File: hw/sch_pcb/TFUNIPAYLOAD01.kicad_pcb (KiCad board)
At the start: 4 copper layers, 90.9 x 50.3 mm, 71 parts, among them J1 SM08B-GHS-TB, J2 HEADER_2x15, J22 HEADER_2x03, J3 SM06B-GHS-TB, J7 SM03B-GHS-TB, M1 HOLE, M2 HOLE, M3 HOLE, M4 HOLE, Q2 BC817-25, Q3 BC817-25, Q4 BC817-25, U10 ATMEGA1284P-AU, U12 MIC5504-3.3YM5-TR, Y1 8 MHz

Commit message: Update schematics. Resolve #2
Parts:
- removed C26, C27, C28, C31, C36, C46, C51: 100nF, Capacitor_SMD:C_0805_2012Metric
- removed C41, C49: 10uF, Capacitor_SMD:C_0805_2012Metric
- removed D11: BZX585-B5V6.115, Diode_SMD:D_SOD-523
- removed F2: SR010-15 100mA, Fuse:Fuse_0805_2012Metric
- removed J22: HEADER_2x03, Mlab_Pin_Headers:SMD_2x03
- removed JP4: Jumper_2_Bridged, NetTie:NetTie-2_SMD_Pad0.5mm
- removed the L1 at (158.5, 101.8)
- removed TP5: Analog GND, TestPoint:TestPoint_Pad_D1.0mm
- removed U12: MIC5504-3.3YM5-TR, Package_TO_SOT_SMD:SOT-23-5
- added C13: 22u, Capacitor_SMD:C_0805_2012Metric, F.Cu at (125.5, 147.2)
- added C14: 47u, Capacitor_SMD:C_0805_2012Metric, F.Cu at (125.5, 150.2)
- added C15: 10u, Capacitor_SMD:C_0805_2012Metric, F.Cu at (125.5, 153.2)
- added C5: 22u, Capacitor_SMD:C_0805_2012Metric, F.Cu at (125.5, 138.1)
- added C6: 47u, Capacitor_SMD:C_0805_2012Metric, F.Cu at (125.5, 141.2)
- added C7: 10u, Capacitor_SMD:C_0805_2012Metric, F.Cu at (125.5, 144.2)
- added D7: RED, LED_SMD:LED_1206_3216Metric, F.Cu at (134.6, 162.0)
- added J3: HEADER_2x03, Mlab_Pin_Headers:SMD_2x03, F.Cu at (134.9, 155.9)
- added J4: SM04B-GHS-TB, Connector_JST:JST_GH_SM04B-GHS-TB_1x04-1MP_P1.25mm_Horizontal, F.Cu at (133.0, 147.8)
- added J6: SM07B-GHS-TB, Connector_JST:JST_GH_SM07B-GHS-TB_1x07-1MP_P1.25mm_Horizontal, F.Cu at (134.9, 140.4)
- added L2: 1uH - DFE252012P-1R0M=P2, Inductor_SMD:L_1008_2520Metric, F.Cu at (145.4, 153.4)
- added L3: 1uH - DFE252012P-1R0M=P2, Inductor_SMD:L_1008_2520Metric, F.Cu at (145.4, 157.2)
- added R10: 511k, Resistor_SMD:R_0805_2012Metric, F.Cu at (121.1, 144.0)
- added R11: 91k, Resistor_SMD:R_0805_2012Metric, F.Cu at (121.1, 147.0)
- added R2: 10k, Resistor_SMD:R_0805_2012Metric, F.Cu at (121.1, 138.1)
- added R22: 806k, Resistor_SMD:R_0805_2012Metric, F.Cu at (121.1, 149.9)
- added R23: 91k, Resistor_SMD:R_0805_2012Metric, F.Cu at (121.1, 152.9)
- added R24: 180R, Resistor_SMD:R_0805_2012Metric, F.Cu at (121.1, 155.8)
- added R25: 100R, Resistor_SMD:R_0603_1608Metric, F.Cu at (129.8, 152.8)
- added R26: 10k, Resistor_SMD:R_0805_2012Metric, F.Cu at (121.1, 158.8)
- added R27: 100R, Resistor_SMD:R_0603_1608Metric, F.Cu at (129.8, 155.3)
- added R28: 100R, Resistor_SMD:R_0603_1608Metric, F.Cu at (129.8, 157.8)
- added R29: 100R, Resistor_SMD:R_0603_1608Metric, F.Cu at (129.8, 160.3)
- added R3: 10k, Resistor_SMD:R_0805_2012Metric, F.Cu at (121.1, 141.1)
- added R30: 100R, Resistor_SMD:R_0603_1608Metric, F.Cu at (129.8, 162.8)
- added SW1: SKRTLAE010, Mlab_SW:SKRT, F.Cu at (141.3, 145.9)
- added SW2: KMT031, Mlab_SW:KMT031 NGJ LHS C&K, F.Cu at (140.4, 153.5)
- added SW3: KMT031, Mlab_SW:KMT031 NGJ LHS C&K, F.Cu at (140.4, 157.5)
- added U1: TPS631000DRLR, Package_TO_SOT_SMD:SOT-583-8, F.Cu at (139.8, 161.5)
- added U3: TPS631000DRLR, Package_TO_SOT_SMD:SOT-583-8, F.Cu at (143.5, 161.5)
- renumbered C38 to C1, C34 to C10, C35 to C11, C39 to C12, C43 to C2, C30 to C3, C33 to C4, C40 to C8, C44 to C9, D6 to D1, D1 to D2, D9 to D3, D7 to D4, D10 to D5, D8 to D6, J3 to J1, J1 to J2, J2 to J5, L2 to L1, Q4 to Q1, R33 to R1, R20 to R12, R21 to R13, R38 to R14, R43 to R15, R37 to R16, R32 to R17, R41 to R18, R45 to R19, R46 to R20, R47 to R21, R34 to R4, R23 to R5, R44 to R6, R42 to R7, R36 to R8, R35 to R9, TP6 to TP1, TP7 to TP2, U10 to U2
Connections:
- net /5v renamed +5V
- net /External_5V renamed Net-(D1-A)
- net /Signal_S&H renamed /EXT_A0
- net /Trace renamed /EXT_B0
- net /Virtual_ground renamed /EXT_A1
- C8 pad 2: GNDA -> GND
- C9 pad 2: GNDA -> GND
- D1 pad 1: Net-(D6-K) (its old number) -> Net-(D1-K)
- J5 pad 10: /RST -> /~{RST}_EXT
- J5 pad 5: /3v3 -> +3.3V
- J5 pad 6: /3v3 -> +3.3V
- J5 pad 8: /connection_detector -> /EXT_DETECTION
- L1 pad 2: Net-(U12-EN) -> +VSW
- U2 pad 1: /PB5 -> /MOSI
- U2 pad 16: POWER_ANALOG_3V3 -> unconnected-(U2-(PCINT31/OC2A)PD7-Pad16)
- U2 pad 2: /PB6 -> /MISO
- U2 pad 3: /PB7 -> /SCLK
- U2 pad 30: unconnected-(U10-(PCINT7/ADC7)PA7-Pad30) -> /BTN_USER_B
- U2 pad 31: unconnected-(U10-(PCINT6/ADC6)PA6-Pad31) -> /BTN_USER_A
- U2 pad 32: unconnected-(U10-(PCINT5/ADC5)PA5-Pad32) -> /#RTS
- U2 pad 33: unconnected-(U10-(PCINT4/ADC4)PA4-Pad33) -> /#CTS
- U2 pad 34: unconnected-(U10-(PCINT3/ADC3)PA3-Pad34) -> /EXT_DETECTION
- U2 pad 35: /Signal -> unconnected-(U2-(PCINT2/ADC2)PA2-Pad35)
- U2 pad 41: unconnected-(U10-(PCINT9/CLKO/T1)PB1-Pad41) -> /EXT_B1
- U2 pad 43: unconnected-(U10-(PCINT11/AIN1/OC0)PB3-Pad43) -> /CS2
- U2 pad 44: /PB4 -> /CS1
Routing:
- net /PB6: track 45.2 -> 0.00 mm, vias 1 -> 0
- net /MISO: track 0.00 -> 45.2 mm, vias 0 -> 1
- net /SCLK: track 0.00 -> 38.0 mm, vias 0 -> 1
- net /PB7: track 38.0 -> 0.00 mm, vias 1 -> 0
- net unconnected-(U10-(PCINT9/CLKO/T1)PB1-Pad41): track 34.5 -> 0.00 mm, vias 2 -> 0
- net /EXT_B1: track 0.00 -> 34.5 mm, vias 0 -> 2
- net (no net): track 147.8 -> 167.7 mm, vias 16 -> 18
- net unconnected-(U2-(PCINT31/OC2A)PD7-Pad16): track 0.00 -> 17.0 mm, vias 0 -> 2
- net POWER_ANALOG_3V3: track 17.0 -> 0.00 mm, vias 2 -> 0
- net +5V: track 16.2 -> 0.00 mm, vias 1 -> 0
- net /PB4: track 8.02 -> 0.00 mm, vias 1 -> 0
- net /CS1: track 0.00 -> 8.02 mm, vias 0 -> 1
- net unconnected-(U2-(PCINT2/ADC2)PA2-Pad35): track 0.00 -> 7.30 mm, vias 0 -> 2
- net /Signal: track 7.30 -> 0.00 mm, vias 2 -> 0
- net /3v3: track 3.79 -> 0.00 mm, vias 1 -> 0
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
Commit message: Fix ERC errors. Fix #3.
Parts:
- removed J7: SM03B-GHS-TB, Connector_JST:JST_GH_SM03B-GHS-TB_1x03-1MP_P1.25mm_Horizontal
- C3, C4: value 15pF -> 15p; moved to F.Cu
- Y1: footprint Mlab_XTAL:Crystal_HC49-4H_Vertical -> Crystal:Crystal_SMD_3225-4Pin_3.2x2.5mm
- moved C4 12.6 mm to (153.1, 70.5)
- moved C3 10.4 mm to (153.1, 67.5), turned to 0 degrees
- moved Y1 9.95 mm to (157.9, 68.3)
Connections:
- C3 pad 1: Net-(U2-XTAL2) -> Net-(U2-XTAL1)
- C4 pad 1: Net-(U2-XTAL1) -> Net-(U2-XTAL2)
- J1 pad 4: unconnected-(J1-Pad4) -> /#RTS
- J1 pad 5: Net-(JP1-B) -> /#CTS
- J5 pad 12: /RX -> /RX1
- J5 pad 14: /TX -> /TX1
- J5 pad 25: /I2C_PWR -> +3.3V
- J5 pad 26: /I2C_PWR -> +3.3V
- JP1 pad 2: Net-(JP1-B) -> /#CTS
- R25 pad 2: /SCK -> /SCLK
- U2 pad 16: unconnected-(U2-(PCINT31/OC2A)PD7-Pad16) -> /C1
- U2 pad 21: unconnected-(U2-(PCINT18/TCK)PC2-Pad21) -> /C0
- U2 pad 27: /AVCC -> +3.3V
- U2 pad 28: GNDA -> GND
- U2 pad 36: /EXT_A1 -> /A1
- U2 pad 37: /EXT_A0 -> /A0
- U2 pad 40: /EXT_B0 -> /B0
- U2 pad 41: /EXT_B1 -> /B1
- Y1 pad 2: Net-(U2-XTAL1) -> GND
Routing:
- net /EXT_B1: track 34.5 -> 0.00 mm, vias 2 -> 0
- net /B1: track 0.00 -> 34.5 mm, vias 0 -> 2
- net GNDA: track 23.5 -> 0.00 mm, vias 18 -> 0
- net GND: track 50.3 -> 72.8 mm, vias 142 -> 159
- net unconnected-(U2-(PCINT31/OC2A)PD7-Pad16): track 17.0 -> 0.00 mm, vias 2 -> 0
- net /C1: track 0.00 -> 17.0 mm, vias 0 -> 2
- net +3.3V: track 144.6 -> 151.8 mm
- net /AVCC: track 7.22 -> 0.00 mm
- net /EXT_A1: track 4.98 -> 0.00 mm, vias 5 -> 0
- net /A1: track 0.00 -> 4.98 mm, vias 0 -> 5
- net Net-(JP1-B): track 4.89 -> 0.00 mm
- net /#CTS: track 0.00 -> 4.89 mm
- net /EXT_A0: track 3.49 -> 0.00 mm, vias 2 -> 0
- net /A0: track 0.00 -> 3.49 mm, vias 0 -> 2
- net /EXT_B0: track 2.81 -> 0.00 mm, vias 2 -> 0
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- removed copper zone on In2.Cu, net GNDA

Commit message: PCB layout WIP.
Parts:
- removed SW3: KMT031, Mlab_SW:KMT031 NGJ LHS C&K
- C13, C14, C15, C3, C4, C5, C6, C7, D3, D4, D5, D6, D7, J3, J4, J6, L2, L3, R10, R11, R2, R22, R23, R24, R25, R26, R27, R28, R29, R3, R30, U1, U3, Y1: moved to B.Cu
- D1: value BZX585-B5V6.115 -> BAS516
- SW1: footprint Mlab_SW:SKRT -> Mlab_SW:KMT031 NGJ LHS C&K; moved to B.Cu
- SW2: value KMT031 -> SKRTLAE010; moved to B.Cu
- moved U3 99.9 mm to (218.0, 94.9)
- moved U1 98.0 mm to (212.9, 96.2), turned to 90 degrees
- moved L3 94.3 mm to (219.8, 99.3)
- moved D7 92.9 mm to (198.9, 94.9)
- moved R24 92.7 mm to (195.6, 100.7)
- moved C15 89.6 mm to (200.0, 103.3)
- moved R23 89.3 mm to (195.6, 103.6)
- moved C14 86.4 mm to (200.0, 106.3)
- moved L2 86.4 mm to (213.2, 99.9)
- moved R22 86.2 mm to (195.6, 106.6)
- moved C13 83.5 mm to (200.0, 109.3)
- moved R11 83.4 mm to (195.6, 109.5)
- moved C7 81.0 mm to (200.0, 112.3)
- moved R10 80.9 mm to (195.6, 112.5)
- moved C6 78.8 mm to (200.0, 115.3)
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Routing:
- net (no net): track 168.8 -> 0.00 mm, vias 19 -> 0
- net +3.3V: track 151.8 -> 0.00 mm, vias 10 -> 0
- net GND: track 72.8 -> 0.00 mm, vias 159 -> 0
- net /SDA: track 69.4 -> 0.00 mm, vias 6 -> 0
- net /SCL: track 68.7 -> 0.00 mm, vias 6 -> 0
- net /~{RST}_PRG: track 47.1 -> 0.00 mm, vias 3 -> 0
- net Vin: track 46.9 -> 0.00 mm, vias 1 -> 0
- net /MISO: track 45.2 -> 0.00 mm, vias 1 -> 0
- net /RX0: track 41.7 -> 0.00 mm, vias 3 -> 0
- net /SCLK: track 38.0 -> 0.00 mm, vias 1 -> 0
- net /TX0: track 36.9 -> 0.00 mm, vias 3 -> 0
- net /B1: track 34.5 -> 0.00 mm, vias 2 -> 0
- net /PC5_D1: track 32.3 -> 0.00 mm, vias 2 -> 0
- net /PC6_D2: track 28.8 -> 0.00 mm, vias 2 -> 0
- net /PC7_D3: track 25.7 -> 0.00 mm, vias 2 -> 0
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- removed copper zone on In1.Cu, net GND
- removed copper zone on In2.Cu, net GND
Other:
- board size 90.9 x 50.3 mm -> 70.6 x 50.3 mm
- copper layers 4 -> 2
- board text removed: "USB RX"
- board text removed: "USB TX"

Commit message: Components placement.
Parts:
- removed FID4, FID5, FID6: Fiducial, Fiducial:Fiducial_1mm_Mask2mm
- FID1, FID2: moved to B.Cu
- J3: footprint Mlab_Pin_Headers:SMD_2x03 -> Mlab_Pin_Headers:SMD_2x03_WO_paste; moved to F.Cu
- moved L2 50.3 mm to (163.0, 97.3), turned to 180 degrees
- moved U1 50.1 mm to (162.9, 100.1), turned to -90 degrees
- moved FID2 48.5 mm to (181.6, 119.6), turned to 90 degrees
- moved L3 44.9 mm to (174.9, 98.3), turned to 180 degrees
- moved C6 44.1 mm to (159.8, 97.2), turned to 90 degrees
- moved U3 43.5 mm to (174.9, 100.9), turned to -90 degrees
- moved C7 42.9 mm to (158.7, 100.6), turned to -90 degrees
- moved C5 39.5 mm to (165.9, 98.2), turned to 90 degrees
- moved R10 36.9 mm to (160.7, 100.5), turned to -90 degrees
- moved R11 34.6 mm to (161.6, 103.1)
- moved SW1 31.8 mm to (151.1, 93.0), turned to 0 degrees
- moved C15 30.2 mm to (169.8, 101.0), turned to -90 degrees
- moved C14 29.0 mm to (171.9, 98.9), turned to 90 degrees
- moved R2 28.2 mm to (151.1, 96.1), turned to 180 degrees
- moved D7 27.7 mm to (173.3, 84.3), turned to -90 degrees
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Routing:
- added copper zone on B.Cu, net +3.3V
- added copper zone on B.Cu, net +VSW
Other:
- board text added: "I2C master"
- board text added: "KAKLIK 2025"
- board text added: "PWR 3V3"
- board text added: "PWR 5V"
- board text added: "SPI master"
- board text added: "TF Payload Connector"
- board text added: "UART Peripheral"
- board text removed: "2023"
- board text removed: "KAKLIK"
- board text removed: "PWR"

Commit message: Footprints updated.
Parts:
- moved R21 17.4 mm to (138.8, 112.0)
- moved R20 11.3 mm to (136.2, 116.0)
- moved C6 8.02 mm to (167.7, 98.7), turned to 0 degrees
- moved R13 6.70 mm to (133.4, 107.0), turned to 0 degrees
- moved C5 6.49 mm to (166.4, 104.7), turned to 0 degrees
- moved C15 6.39 mm to (174.4, 96.5), turned to 180 degrees
- moved L2 6.20 mm to (167.2, 101.8), turned to 90 degrees
- moved C7 6.17 mm to (164.1, 97.5), turned to 180 degrees
- moved C13 5.77 mm to (176.3, 104.6), turned to 0 degrees
- moved C14 4.60 mm to (176.5, 98.6), turned to 0 degrees
- moved R12 4.01 mm to (133.5, 109.5), turned to 0 degrees
- moved L3 4.00 mm to (177.1, 101.6), turned to 90 degrees
- moved R22 3.91 mm to (173.0, 98.6), turned to 180 degrees
- moved R10 3.67 mm to (164.2, 99.4), turned to 180 degrees
- moved R23 3.41 mm to (172.0, 101.4), turned to -90 degrees
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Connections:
- J4 pad 1: +5V -> +VSW
- J6 pad 1: +5V -> +VSW
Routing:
- net +VSW: track 0.00 -> 52.7 mm
- net /SDA: track 0.00 -> 30.8 mm, vias 0 -> 2
- net /#RTS: track 0.00 -> 29.8 mm, vias 0 -> 2
- net /SCL: track 0.00 -> 29.7 mm
- net /#CTS: track 0.00 -> 29.7 mm, vias 0 -> 2
- net Net-(J2-Pad7): track 0.00 -> 26.7 mm
- net /MOSI: track 0.00 -> 26.1 mm, vias 0 -> 2
- net /CS1: track 0.00 -> 23.4 mm, vias 0 -> 2
- net /CS2: track 0.00 -> 23.1 mm, vias 0 -> 2
- net /RX0: track 0.00 -> 20.1 mm, vias 0 -> 2
- net Net-(J2-Pad6): track 0.00 -> 19.5 mm
- net /TX0: track 0.00 -> 19.3 mm, vias 0 -> 2
- net /GEO_STAT: track 0.00 -> 19.1 mm
- net /SCLK: track 0.00 -> 19.0 mm, vias 0 -> 1
- net /MISO: track 0.00 -> 18.7 mm, vias 0 -> 1
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
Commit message: Routing.
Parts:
- moved C4 4.34 mm to (142.0, 118.5), turned to 180 degrees
- moved C8 2.49 mm to (143.8, 92.9)
- moved C9 1.80 mm to (144.3, 95.1)
- moved R3 1.78 mm to (153.9, 96.8), turned to 90 degrees
- moved C2 1.44 mm to (149.4, 112.4), turned to -90 degrees
- moved JP1 1.16 mm to (150.3, 122.2), turned to 0 degrees
- moved SW2 1.04 mm to (154.4, 92.8), turned to -90 degrees
- moved R5 0.85 mm to (147.5, 112.4)
- moved C10 0.50 mm to (145.2, 112.4), turned to -90 degrees
- moved SW1 0.18 mm to (151.2, 92.8), turned to -90 degrees
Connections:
- net /#CTS renamed /~{CTS}
- net /#RTS renamed /~{RTS}
- J3 pad 5: /RST#_P -> /~{RST}_PRG
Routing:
- net /SDA: track 30.8 -> 68.9 mm, vias 2 -> 3
- net /SCL: track 29.7 -> 64.3 mm, vias 0 -> 1
- net /TX1: track 8.69 -> 39.1 mm, vias 0 -> 1
- net /RX1: track 2.98 -> 28.9 mm, vias 0 -> 1
- net +3.3V: track 12.4 -> 35.8 mm
- net /EXT_DETECTION: track 0.00 -> 23.0 mm, vias 0 -> 2
- net /BTN_USER_B: track 0.00 -> 17.7 mm
- net /~{RST}_PRG: track 0.00 -> 16.6 mm, vias 0 -> 1
- net /MISO: track 18.7 -> 31.9 mm, vias 1 -> 2
- net Net-(U2-XTAL2): track 0.00 -> 10.5 mm
- net /BTN_USER_A: track 0.00 -> 9.32 mm
- net Net-(U2-XTAL1): track 0.00 -> 8.59 mm
- net Net-(U2-AREF): track 0.00 -> 5.00 mm
- net Net-(J2-Pad1): track 0.00 -> 3.21 mm
- net Net-(J2-Pad3): track 0.00 -> 2.70 mm
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
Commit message: Pinheader correctly positioned.
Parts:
- removed Q3: BC817-25, Package_TO_SOT_SMD:SOT-23
- removed R16: 10k, Resistor_SMD:R_0805_2012Metric
- D3, D4, D5, D6, D7: footprint LED_SMD:LED_1206_3216Metric -> Mlab_D:LED_1206_mill
- J5: footprint Connector_PinSocket_2.54mm:PinSocket_2x15_P2.54mm_Vertical -> Mlab_Pin_Headers:Straight_2x15
- moved J5 17.5 mm to (148.5, 83.4)
- moved L1 6.79 mm to (160.8, 122.0), turned to -90 degrees
- moved R6 4.55 mm to (120.5, 98.3)
- moved R8 4.53 mm to (120.4, 94.0)
- moved R15 4.50 mm to (120.6, 103.0), turned to 0 degrees
- moved R7 4.49 mm to (128.7, 97.3)
- moved R9 4.14 mm to (128.6, 93.1)
- moved Q1 3.94 mm to (124.4, 98.2), turned to 180 degrees
- moved Q2 3.80 mm to (124.3, 94.0), turned to 180 degrees
- moved D2 2.35 mm to (159.3, 121.5), turned to -90 degrees
- moved C1 1.97 mm to (158.8, 119.2)
- moved R23 1.42 mm to (171.4, 100.1)
- moved R22 1.30 mm to (174.1, 99.3)
- moved C14 0.94 mm to (177.5, 98.6)
- moved C15 0.93 mm to (174.1, 97.4)
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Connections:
- D3 pad 2: Vin -> +5V
- D4 pad 2: Vin -> +5V
- D6 pad 1: Net-(D6-K) -> GND
- D6 pad 2: +3.3V -> Net-(D6-A)
- R15 pad 1: Net-(Q3-C) -> Net-(D6-A)
- R15 pad 2: Net-(D6-K) -> /PC7_D3
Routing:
- net +VSW: track 52.7 -> 70.7 mm
- net Net-(D1-K): track 5.48 -> 0.00 mm
- added copper zone on B.Cu, net +5V

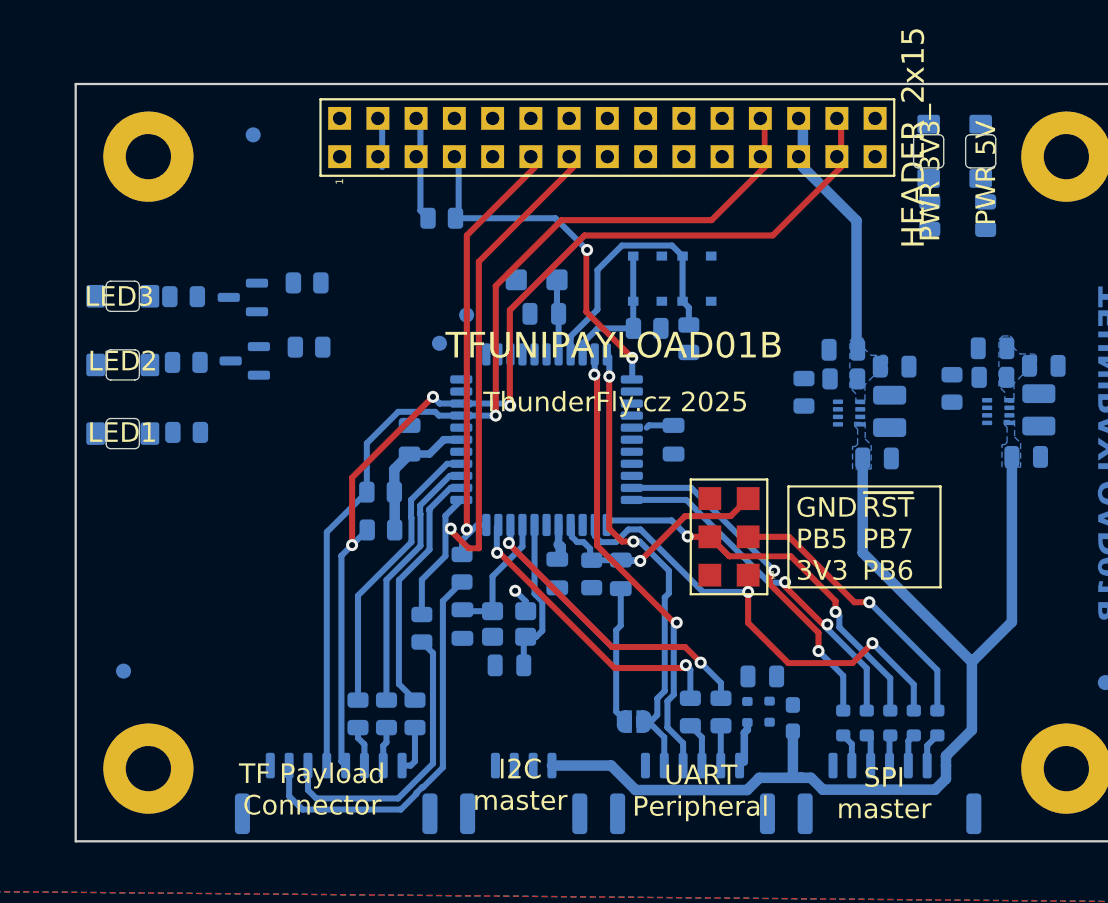
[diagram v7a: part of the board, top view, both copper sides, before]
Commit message: Pinheader changed to footprint with square pads. Routing more nets.
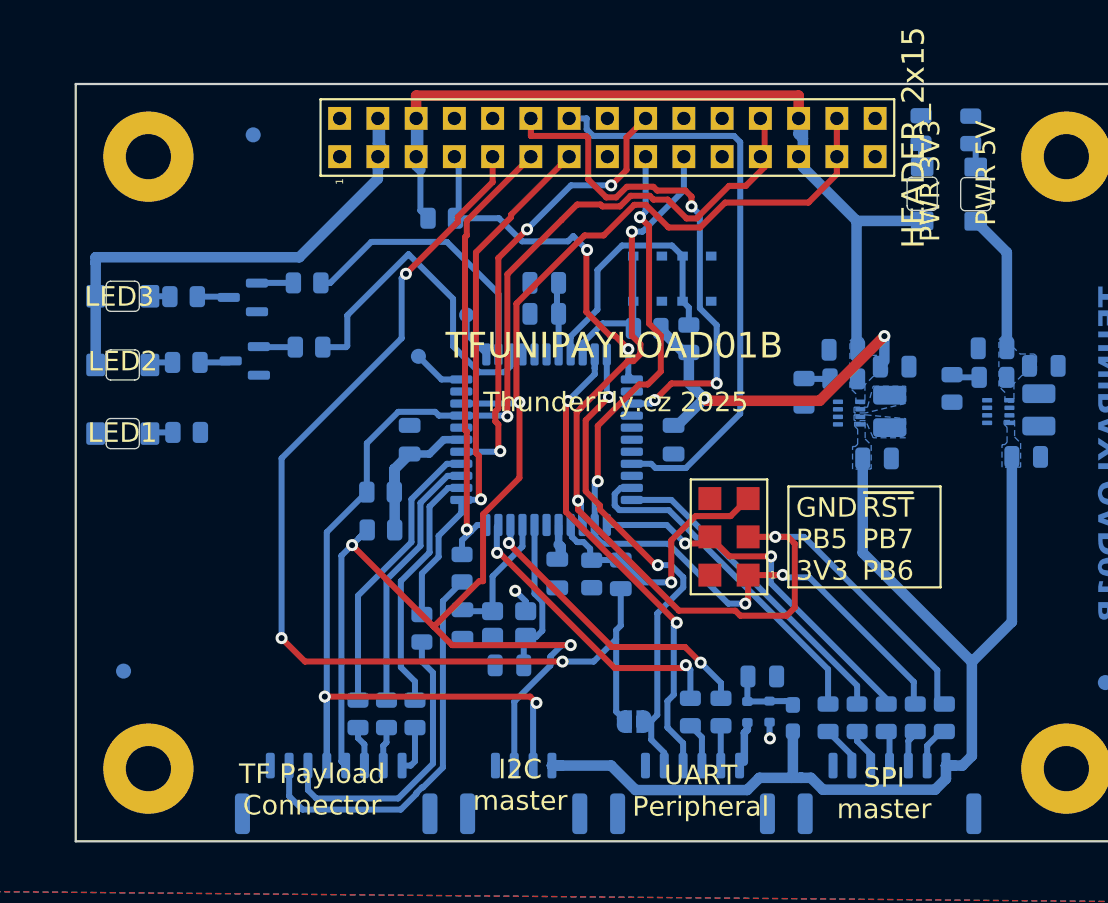
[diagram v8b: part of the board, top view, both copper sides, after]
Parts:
- C8: value 10uF -> 10u; footprint Capacitor_Tantalum_SMD:CP_EIA-3216-18_Kemet-A -> Capacitor_SMD:C_0805_2012Metric
- R25, R27, R28, R29, R30: footprint Resistor_SMD:R_0603_1608Metric -> Resistor_SMD:R_0805_2012Metric
- moved R24 5.78 mm to (172.6, 82.9), turned to 90 degrees
- moved R14 5.74 mm to (169.3, 82.9), turned to 90 degrees
- moved D7 2.86 mm to (173.0, 87.2), turned to 90 degrees
- moved D5 2.85 mm to (169.4, 87.1), turned to 90 degrees
- moved TP1 1.64 mm to (136.0, 97.9)
- moved R30 1.07 mm to (163.2, 121.9)
- moved R29 0.73 mm to (165.1, 121.9)
- moved R25 0.58 mm to (170.9, 121.9)
- moved C8 0.55 mm to (144.3, 93.1)
- moved R28 0.44 mm to (167.0, 121.9)
- moved R27 0.36 mm to (168.9, 121.9)
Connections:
- J5 pad 10: /~{RST}_EXT -> /A0
- J5 pad 11: /A1 -> /RX1
- J5 pad 12: /RX1 -> /A1
- J5 pad 13: /B1 -> /TX1
- J5 pad 14: /TX1 -> /B1
- J5 pad 15: /B0 -> /MOSI
- J5 pad 16: /MOSI -> /B0
- J5 pad 17: /C1 -> /MISO
- J5 pad 18: /MISO -> /C1
- J5 pad 19: /C0 -> /SCLK
- J5 pad 20: /SCLK -> /C0
- J5 pad 7: GND -> /EXT_DETECTION
- J5 pad 8: /EXT_DETECTION -> GND
- J5 pad 9: /A0 -> /~{RST}_EXT
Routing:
- net +3.3V: track 35.8 -> 97.3 mm, vias 0 -> 2
- net /~{RST}_EXT: track 9.18 -> 70.3 mm, vias 0 -> 3
- net /SCLK: track 19.0 -> 70.5 mm, vias 1 -> 3
- net +5V: track 2.54 -> 44.9 mm
- net /B1: track 0.00 -> 39.3 mm
- net /A1: track 0.00 -> 35.0 mm, vias 0 -> 3
- net /SDA: track 68.9 -> 102.3 mm
- net /C1: track 0.00 -> 30.5 mm, vias 0 -> 3
- net /SCL: track 64.3 -> 89.7 mm, vias 1 -> 3
- net /MISO: track 31.9 -> 57.2 mm, vias 2 -> 4
- net /PC6_D2: track 0.00 -> 22.3 mm
- net /PC5_D1: track 0.00 -> 18.4 mm
- net Net-(D1-K): track 0.00 -> 4.75 mm
- net Net-(U2-PC3): track 0.00 -> 3.48 mm
- net /TX1: track 39.1 -> 35.9 mm
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- added copper zone on B.Cu, net Net-(U1-LX1)
- added copper zone on B.Cu, net Net-(U1-LX2)
